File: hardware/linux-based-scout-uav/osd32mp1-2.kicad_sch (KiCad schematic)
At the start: 1 part, among them U1 OSD32MP157C-512M-IAA

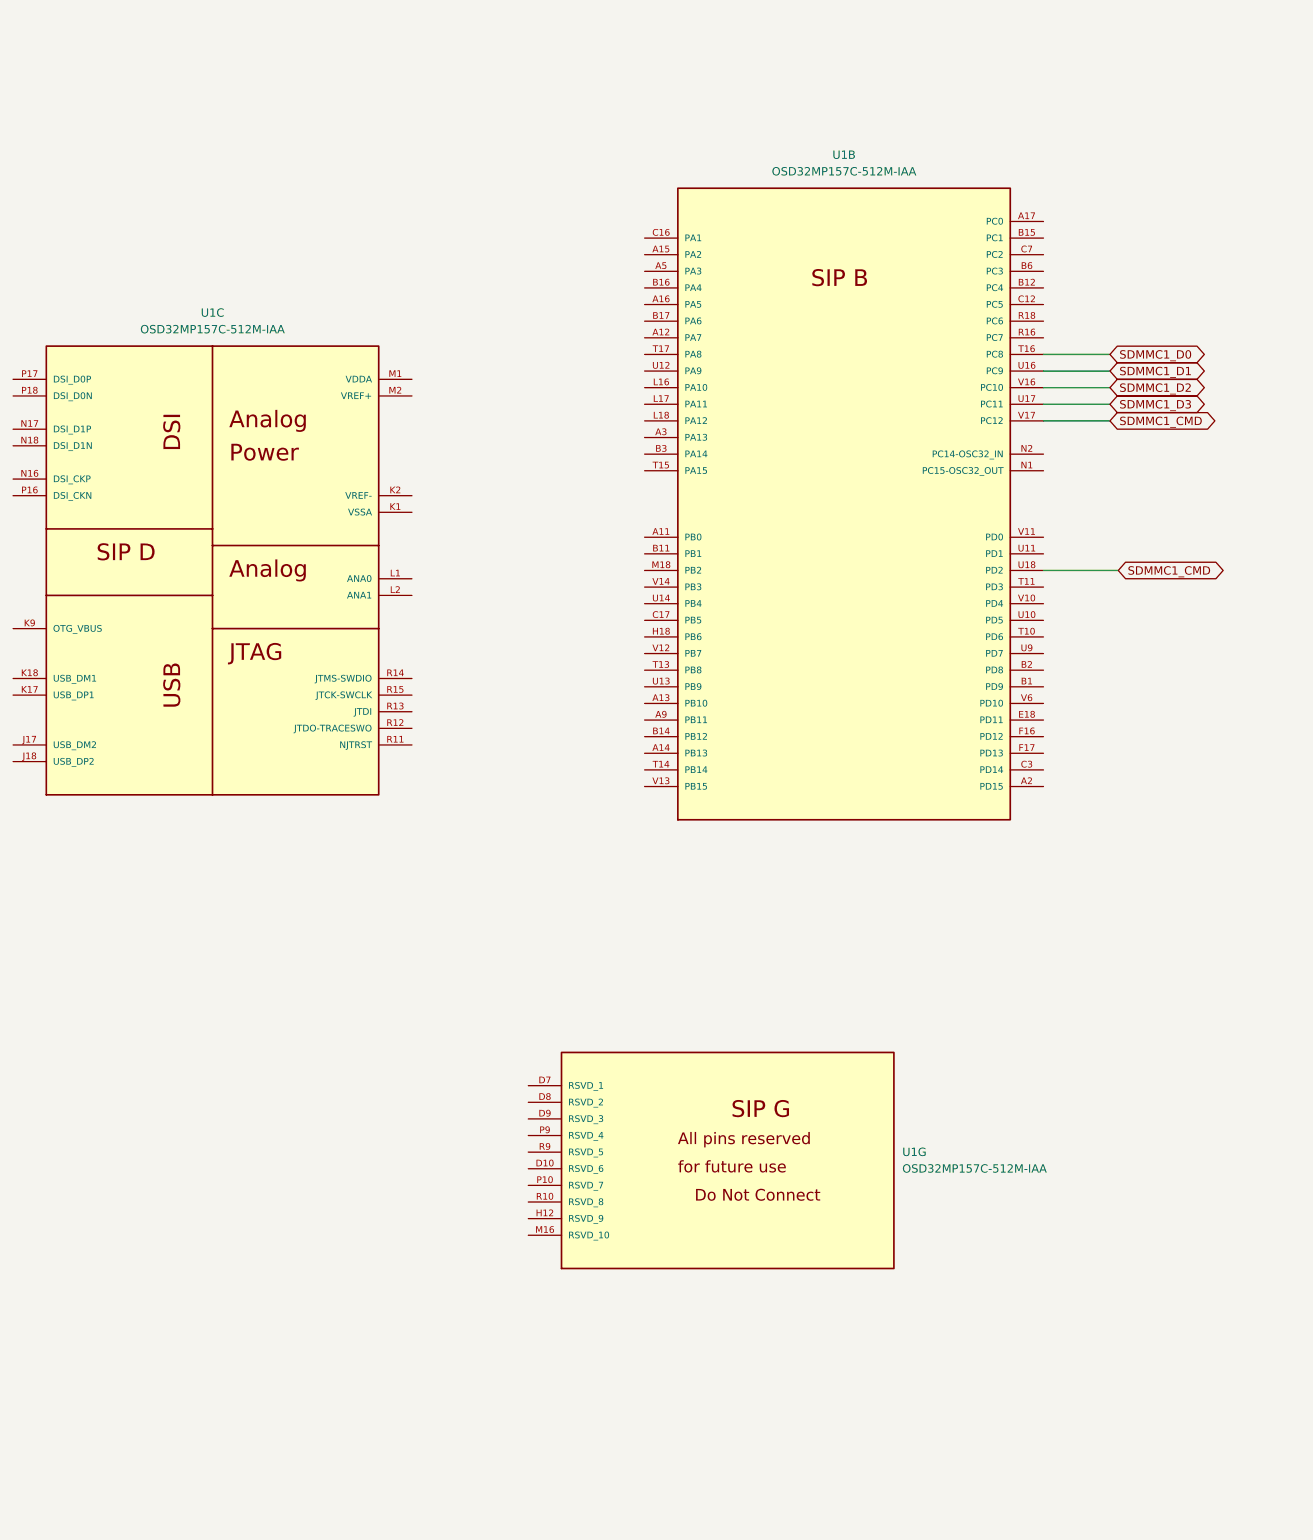
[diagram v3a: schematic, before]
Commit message: Schematic updates
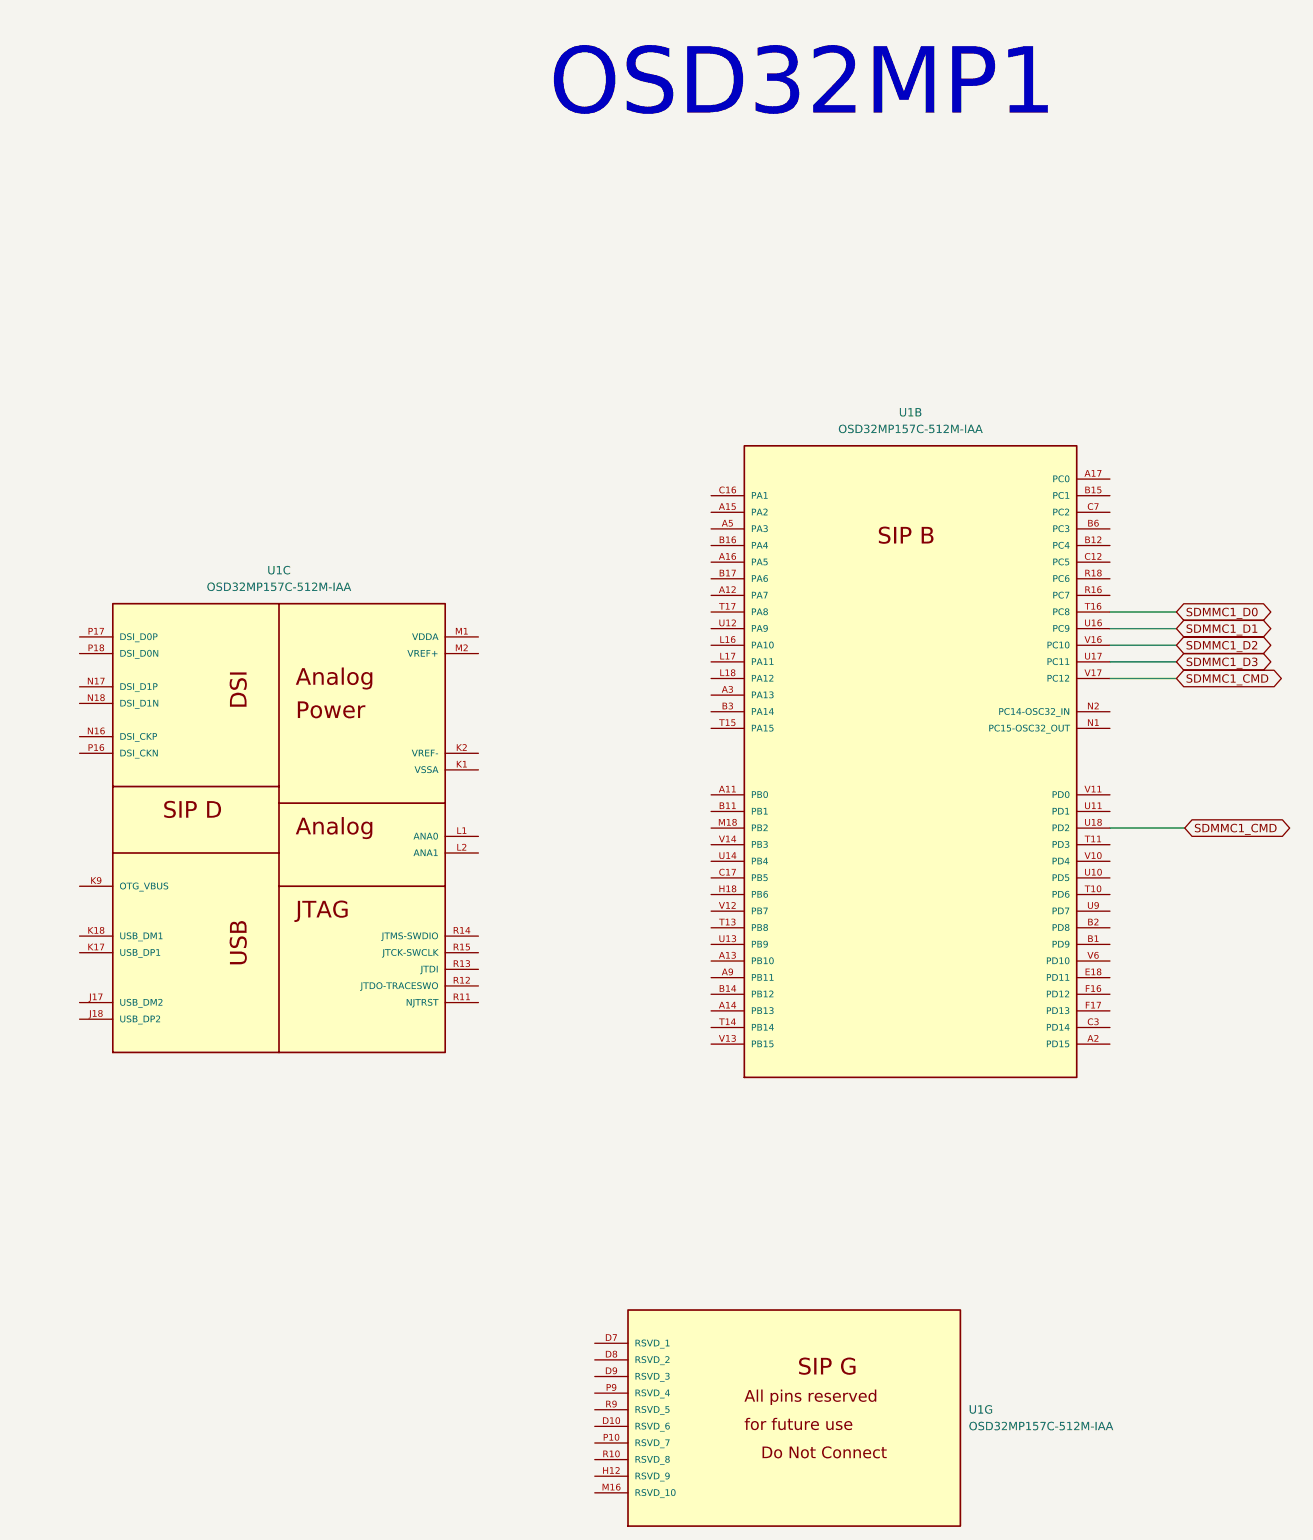
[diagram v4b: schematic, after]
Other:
- note added: "OSD32MP1"
- moved on the sheet: U1B, U1C, U1G
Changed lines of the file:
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@@
 	(wire
 		(pts
-			(xy 241.3 97.79) (xy 252.73 97.79)
+			(xy 251.46 137.16) (xy 262.89 137.16)
 		)
 		(stroke
@@
 	(wire
 		(pts
-			(xy 241.3 67.31) (xy 251.46 67.31)
+			(xy 251.46 106.68) (xy 261.62 106.68)
 		)
 		(stroke
@@
 	(wire
 		(pts
-			(xy 241.3 64.77) (xy 251.46 64.77)
+			(xy 251.46 104.14) (xy 261.62 104.14)
 		)
 		(stroke
@@
 	(wire
 		(pts
-			(xy 241.3 69.85) (xy 251.46 69.85)
+			(xy 251.46 109.22) (xy 261.62 109.22)
 		)
 		(stroke
@@
 	(wire
 		(pts
-			(xy 241.3 72.39) (xy 251.46 72.39)
+			(xy 251.46 111.76) (xy 261.62 111.76)
 		)
 		(stroke
@@
 	(wire
 		(pts
-			(xy 241.3 74.93) (xy 251.46 74.93)
+			(xy 251.46 114.3) (xy 261.62 114.3)
 		)
 		(stroke
@@
 		)
 	)
+	(text "OSD32MP1"
+		(exclude_from_sim no)
+		(at 204.47 23.368 0)
+		(effects
+			(font
+				(size 10.16 10.16)
+			)
+		)
+	)
 	(global_label "SDMMC1_CMD"
 		(shape bidirectional)
-		(at 251.46 74.93 0)
+		(at 261.62 114.3 0)
 		(fields_autoplaced yes)
 		(effects
@@
 		)
 		(property "Intersheetrefs" "${INTERSHEET_REFS}"
-			(at 268.3773 74.93 0)
+			(at 278.5373 114.3 0)
 			(show_name yes)
 			(effects
@@
 	(global_label "SDMMC1_D2"
 		(shape bidirectional)
-		(at 251.46 69.85 0)
+		(at 261.62 109.22 0)
 		(fields_autoplaced yes)
 		(effects
@@
 		)
 		(property "Intersheetrefs" "${INTERSHEET_REFS}"
-			(at 266.8654 69.85 0)
+			(at 277.0254 109.22 0)
 			(effects
 				(font
@@
 	(global_label "SDMMC1_D1"
 		(shape bidirectional)
-		(at 251.46 67.31 0)
+		(at 261.62 106.68 0)
 		(fields_autoplaced yes)
 		(effects
@@
 		)
 		(property "Intersheetrefs" "${INTERSHEET_REFS}"
-			(at 266.8654 67.31 0)
+			(at 277.0254 106.68 0)
 			(effects
 				(font
@@
 	(global_label "SDMMC1_D0"
 		(shape bidirectional)
-		(at 251.46 64.77 0)
+		(at 261.62 104.14 0)
 		(fields_autoplaced yes)
 		(effects
@@
 		)
 		(property "Intersheetrefs" "${INTERSHEET_REFS}"
-			(at 266.8654 64.77 0)
+			(at 277.0254 104.14 0)
 			(effects
 				(font
@@
 	(global_label "SDMMC1_D3"
 		(shape bidirectional)
-		(at 251.46 72.39 0)
+		(at 261.62 111.76 0)
 		(fields_autoplaced yes)
 		(effects
@@
 		)
 		(property "Intersheetrefs" "${INTERSHEET_REFS}"
-			(at 266.8654 72.39 0)
+			(at 277.0254 111.76 0)
 			(effects
 				(font
@@
 	(global_label "SDMMC1_CMD"
 		(shape bidirectional)
-		(at 252.73 97.79 0)
+		(at 262.89 137.16 0)
 		(fields_autoplaced yes)
 		(effects
@@
 		)
 		(property "Intersheetrefs" "${INTERSHEET_REFS}"
-			(at 269.6473 97.79 0)
+			(at 279.8073 137.16 0)
 			(show_name yes)
 			(effects
@@
 	(symbol
 		(lib_id "OSD32MP157C-512M-IAA:OSD32MP157C-512M-IAA")
-		(at 167.64 204.47 0)
+		(at 177.8 243.84 0)
 		(unit 7)
 		(exclude_from_sim no)
@@
 		(fields_autoplaced yes)
 		(property "Reference" "U1"
-			(at 219.71 186.6899 0)
+			(at 229.87 226.0599 0)
 			(effects
 				(font
@@
 		)
 		(property "Value" "OSD32MP157C-512M-IAA"
-			(at 219.71 189.2299 0)
+			(at 229.87 228.5999 0)
 			(effects
 				(font
@@
 		)
 		(property "Footprint" "OSD32MP157C-512M-IAA:OSD32MP15X-BGA-324"
-			(at 167.64 204.47 0)
+			(at 177.8 243.84 0)
 			(effects
 				(font
@@
 		)
 		(property "Datasheet" ""
-			(at 167.64 204.47 0)
+			(at 177.8 243.84 0)
 			(effects
 				(font
@@
 		)
 		(property "Description" ""
-			(at 167.64 204.47 0)
+			(at 177.8 243.84 0)
 			(effects
 				(font
@@
 		)
 		(property "MF" "Octavo Systems LLC"
-			(at 167.64 204.47 0)
+			(at 177.8 243.84 0)
 			(effects
 				(font
@@
 		)
 		(property "Description_1" "\nOSD32MP15x Embedded Module Arm® Dual Cortex®-A7, Arm® Cortex®-M4 NEON™ SIMD 650MHz, 209MHz\n"
-			(at 167.64 204.47 0)
+			(at 177.8 243.84 0)
 			(effects
 				(font
@@
 		)
 		(property "Package" "BGA-302 Octavo Systems"
-			(at 167.64 204.47 0)
+			(at 177.8 243.84 0)
 			(effects
 				(font
@@
 		)
 		(property "Price" "None"
-			(at 167.64 204.47 0)
+			(at 177.8 243.84 0)
 			(effects
 				(font
@@
 		)
 		(property "SnapEDA_Link" "https://www.snapeda.com/parts/OSD32MP157C-512M-IAA/Octavo+Systems+LLC/view-part/?ref=snap"
-			(at 167.64 204.47 0)
+			(at 177.8 243.84 0)
 			(effects
 				(font
@@
 		)
 		(property "MP" "OSD32MP157C-512M-IAA"
-			(at 167.64 204.47 0)
+			(at 177.8 243.84 0)
 			(effects
 				(font
@@
 		)
 		(property "Purchase-URL" "https://www.snapeda.com/api/url_track_click_mouser/?unipart_id=4998964&manufacturer=Octavo Systems LLC&part_name=OSD32MP157C-512M-IAA&search_term=osd32mp1"
-			(at 167.64 204.47 0)
+			(at 177.8 243.84 0)
 			(effects
 				(font
@@
 		)
 		(property "Availability" "In Stock"
-			(at 167.64 204.47 0)
+			(at 177.8 243.84 0)
 			(effects
 				(font
@@
 		)
 		(property "Check_prices" "https://www.snapeda.com/parts/OSD32MP157C-512M-IAA/Octavo+Systems+LLC/view-part/?ref=eda"
-			(at 167.64 204.47 0)
+			(at 177.8 243.84 0)
 			(effects
 				(font
@@
 	(symbol
 		(lib_id "OSD32MP157C-512M-IAA:OSD32MP157C-512M-IAA")
-		(at 88.9 132.08 0)
+		(at 99.06 171.45 0)
 		(unit 3)
 		(exclude_from_sim no)
@@
 		(fields_autoplaced yes)
 		(property "Reference" "U1"
-			(at 114.3 58.42 0)
+			(at 124.46 97.79 0)
 			(effects
 				(font
@@
 		)
 		(property "Value" "OSD32MP157C-512M-IAA"
-			(at 114.3 60.96 0)
+			(at 124.46 100.33 0)
 			(effects
 				(font
@@
 		)
 		(property "Footprint" "OSD32MP157C-512M-IAA:OSD32MP15X-BGA-324"
-			(at 88.9 132.08 0)
+			(at 99.06 171.45 0)
 			(effects
 				(font
@@
 		)
 		(property "Datasheet" ""
-			(at 88.9 132.08 0)
+			(at 99.06 171.45 0)
 			(effects
 				(font
@@
 		)
 		(property "Description" ""
-			(at 88.9 132.08 0)
+			(at 99.06 171.45 0)
 			(effects
 				(font
@@
 		)
 		(property "MF" "Octavo Systems LLC"
-			(at 88.9 132.08 0)
+			(at 99.06 171.45 0)
 			(effects
 				(font
@@
 		)
 		(property "Description_1" "\nOSD32MP15x Embedded Module Arm® Dual Cortex®-A7, Arm® Cortex®-M4 NEON™ SIMD 650MHz, 209MHz\n"
-			(at 88.9 132.08 0)
+			(at 99.06 171.45 0)
 			(effects
 				(font
@@
 		)
 		(property "Package" "BGA-302 Octavo Systems"
-			(at 88.9 132.08 0)
+			(at 99.06 171.45 0)
 			(effects
 				(font
@@
 		)
 		(property "Price" "None"
-			(at 88.9 132.08 0)
+			(at 99.06 171.45 0)
 			(effects
 				(font
@@
 		)
 		(property "SnapEDA_Link" "https://www.snapeda.com/parts/OSD32MP157C-512M-IAA/Octavo+Systems+LLC/view-part/?ref=snap"
-			(at 88.9 132.08 0)
+			(at 99.06 171.45 0)
 			(effects
 				(font
@@
 		)
 		(property "MP" "OSD32MP157C-512M-IAA"
-			(at 88.9 132.08 0)
+			(at 99.06 171.45 0)
 			(effects
 				(font
@@
 		)
 		(property "Purchase-URL" "https://www.snapeda.com/api/url_track_click_mouser/?unipart_id=4998964&manufacturer=Octavo Systems LLC&part_name=OSD32MP157C-512M-IAA&search_term=osd32mp1"
-			(at 88.9 132.08 0)
+			(at 99.06 171.45 0)
 			(effects
 				(font
@@
 		)
 		(property "Availability" "In Stock"
-			(at 88.9 132.08 0)
+			(at 99.06 171.45 0)
 			(effects
 				(font
@@
 		)
 		(property "Check_prices" "https://www.snapeda.com/parts/OSD32MP157C-512M-IAA/Octavo+Systems+LLC/view-part/?ref=eda"
-			(at 88.9 132.08 0)
+			(at 99.06 171.45 0)
 			(effects
 				(font
@@
 	(symbol
 		(lib_id "OSD32MP157C-512M-IAA:OSD32MP157C-512M-IAA")
-		(at 185.42 135.89 0)
+		(at 195.58 175.26 0)
 		(unit 2)
 		(exclude_from_sim no)
@@
 		(fields_autoplaced yes)
 		(property "Reference" "U1"
-			(at 210.82 34.29 0)
+			(at 220.98 73.66 0)
 			(effects
 				(font
@@
 		)
 		(property "Value" "OSD32MP157C-512M-IAA"
-			(at 210.82 36.83 0)
+			(at 220.98 76.2 0)
 			(effects
 				(font
@@
 		)
 		(property "Footprint" "OSD32MP157C-512M-IAA:OSD32MP15X-BGA-324"
-			(at 185.42 135.89 0)
+			(at 195.58 175.26 0)
 			(effects
 				(font
@@
 		)
 		(property "Datasheet" ""
-			(at 185.42 135.89 0)
+			(at 195.58 175.26 0)
 			(effects
 				(font
@@
 		)
 		(property "Description" ""
-			(at 185.42 135.89 0)
+			(at 195.58 175.26 0)
 			(effects
 				(font
@@
 		)
 		(property "MF" "Octavo Systems LLC"
-			(at 185.42 135.89 0)
+			(at 195.58 175.26 0)
 			(effects
 				(font
@@
 		)
 		(property "Description_1" "\nOSD32MP15x Embedded Module Arm® Dual Cortex®-A7, Arm® Cortex®-M4 NEON™ SIMD 650MHz, 209MHz\n"
-			(at 185.42 135.89 0)
+			(at 195.58 175.26 0)
 			(effects
 				(font
@@
 		)
 		(property "Package" "BGA-302 Octavo Systems"
-			(at 185.42 135.89 0)
+			(at 195.58 175.26 0)
 			(effects
 				(font
@@
 		)
 		(property "Price" "None"
-			(at 185.42 135.89 0)
+			(at 195.58 175.26 0)
 			(effects
 				(font
@@
 		)
 		(property "SnapEDA_Link" "https://www.snapeda.com/parts/OSD32MP157C-512M-IAA/Octavo+Systems+LLC/view-part/?ref=snap"
-			(at 185.42 135.89 0)
+			(at 195.58 175.26 0)
 			(effects
 				(font
@@
 		)
 		(property "MP" "OSD32MP157C-512M-IAA"
-			(at 185.42 135.89 0)
+			(at 195.58 175.26 0)
 			(effects
 				(font
@@
 		)
 		(property "Purchase-URL" "https://www.snapeda.com/api/url_track_click_mouser/?unipart_id=4998964&manufacturer=Octavo Systems LLC&part_name=OSD32MP157C-512M-IAA&search_term=osd32mp1"
-			(at 185.42 135.89 0)
+			(at 195.58 175.26 0)
 			(effects
 				(font
@@
 		)
 		(property "Availability" "In Stock"
-			(at 185.42 135.89 0)
+			(at 195.58 175.26 0)
 			(effects
 				(font
@@
 		)
 		(property "Check_prices" "https://www.snapeda.com/parts/OSD32MP157C-512M-IAA/Octavo+Systems+LLC/view-part/?ref=eda"
-			(at 185.42 135.89 0)
-			(effects
-				(font
+			(at 195.58 175.26 0)
+			(effects
+				(font

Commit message: Schematic update
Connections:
- net I2C1_SCL: now reaches U1.H18 (PB6)
- net I2C1_SDA: now reaches U1.V12 (PB7)
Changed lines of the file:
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@@
+	(wire
+		(pts
+			(xy 177.8 147.32) (xy 190.5 147.32)
+		)
+		(stroke
+			(width 0)
+			(type default)
+		)
+	)
+	(wire
+		(pts
+			(xy 177.8 149.86) (xy 190.5 149.86)
+		)
+		(stroke
+			(width 0)
+			(type default)
+		)
+	)
 	(wire
 		(pts
@@
 				(hide yes)
 			)
+		)
+	)
+	(global_label "I2C1_SCL"
+		(shape output)
+		(at 177.8 147.32 180)
+		(fields_autoplaced yes)
+		(effects
+			(font
+				(size 1.27 1.27)
+			)
+			(justify right)
+		)
+		(property "Intersheetrefs" "${INTERSHEET_REFS}"
+			(at 166.0458 147.32 0)
+			(effects
+				(font
+					(size 1.27 1.27)
+				)
+				(justify right)
+				(hide yes)
+			)
+		)
+	)
+	(global_label "I2C1_SDA"
+		(shape bidirectional)
+		(at 177.8 149.86 180)
+		(fields_autoplaced yes)
+		(effects
+			(font
+				(size 1.27 1.27)
+			)
+			(justify right)
+		)
+		(property "Intersheetrefs" "${INTERSHEET_REFS}"
+			(at 164.874 149.86 0)
+			(effects
+				(font
+					(size 1.27 1.27)
+				)
+				(justify right)
+				(hide yes)
+			)

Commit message: Schematic update
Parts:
- added R8, R9: Jumper, Resistor_SMD:R_0402_1005Metric, symbol Device:R
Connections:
- net USB_DM2: now reaches U1.J17 (USB_DM2)
- net USB_DP2: now reaches U1.J18 (USB_DP2)
- net at U1.K1 (VSSA): now also R9.2
- net USB_DP1: now reaches U1.K17 (USB_DP1)
- net USB_DM1: now reaches U1.K18 (USB_DM1)
- net at U1.K2 (VREF-): now also R9.1
- net at U1.M1 (VDDA): now also R8.1
- net at U1.M2 (VREF+): now also R8.2
- net ~{TRST}: now reaches U1.R11 (NJTRST)
- net SWO/TDO: now reaches U1.R12 (JTDO-TRACESWO)
- net TDI: now reaches U1.R13 (JTDI)
- net SWDIO/TMS: now reaches U1.R14 (JTMS-SWDIO)
- net SWCLK/TCK: now reaches U1.R15 (JTCK-SWCLK)
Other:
- moved on the sheet: U1C

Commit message: Schematic update
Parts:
- added C1, C2: C, Capacitor_SMD:C_0402_1005Metric, symbol Device:C
- added J3: TC2050-IDC-NL, TC2050-IDC-NL:TAG-CONNECT_TC2050-IDC-NL, symbol TC2050-IDC-NL:TC2050-IDC-NL
- added Y1: ABS05-32.768KHZ-7-T, ABS05-32.768KHZ-7-T:XTAL_ABS05-32.768KHZ-7-T, symbol ABS05-32.768KHZ-7-T:ABS05-32.768KHZ-7-T
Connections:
- net SWCLK/TCK: now also J3.4
- net SWDIO/TMS: now also J3.2
- net SWO/TDO: now also J3.6
- net TDI: now also J3.8
- net ~{TRST}: now also J3.9
- net at U1.N1 (PC15-OSC32_OUT): now also C2.1, Y1.1
- net at U1.N2 (PC14-OSC32_IN): now also C1.1, Y1.2
- new net +3V3: J3.1
- new net GND: C1.2, C2.2, J3.3
- new net ~{RESET}: J3.10

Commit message: Schematic update
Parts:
- C1, C2: value C -> 12pF
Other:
- note added: "Do not connect"
- note added: "JTAG"
- moved on the sheet: J3, U1G
